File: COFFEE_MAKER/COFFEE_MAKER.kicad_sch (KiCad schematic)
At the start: 8 parts, among them U1 AZ1117IH-3.3TRG1, U2 AZ1117IH-5TRG1

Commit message: updated schematics
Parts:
- added C10, C9: C, symbol Device:C
- added C13, C14: C_Polarized_US, symbol Device:C_Polarized_US
- added C16: 100nF, symbol Device:C
- added C17: 10uF, symbol Device:C
- added C18, C20, C21: .1uF, symbol Device:C
- added C19: 1uF, symbol Device:C
- added D1: LED, symbol Device:LED
- added D7, D8: 1N4148, Diode_THT:D_DO-35_SOD27_P7.62mm_Horizontal, symbol Diode:1N4148
- added DS1: HY1602E, Display:HY1602E, symbol Display_Character:HY1602E
- added FB1, FB2: FerriteBead_Small, symbol Device:FerriteBead_Small
- added J2: Conn_01x06, symbol Connector_Generic:Conn_01x06
- added J3, J6: Conn_01x02_Pin, Connector_PinHeader_2.54mm:PinHeader_1x02_P2.54mm_Vertical, symbol Connector:Conn_01x02_Pin
- added J4: Screw_Terminal_01x02, symbol Connector:Screw_Terminal_01x02
- added J5: USB_C_Receptacle_USB2.0, symbol Connector:USB_C_Receptacle_USB2.0
- added J7: Conn_01x04, symbol Connector_Generic:Conn_01x04
- added JP1: A0, symbol Jumper:SolderJumper_2_Open
- added JP2: A1, symbol Jumper:SolderJumper_2_Open
- added JP3: A2, symbol Jumper:SolderJumper_2_Open
- added JP4: Jumper_2_Open, symbol Jumper:Jumper_2_Open
- added Q1: BC850, Package_TO_SOT_SMD:SOT-23, symbol Transistor_BJT:BC850
- added R10: 10k, symbol Device:R
- added R11, R12, R13, R14, R3, R4, R5, R6, R7: R, symbol Device:R
- added R8, R9: 5.1 k, symbol Device:R
- added RV1: potentiometer, Potentiometer_SMD:Potentiometer_ACP_CA9-VSMD_Vertical_Hole, symbol Device:R_Potentiometer_Trim
- added SW5: Reset, symbol Switch:SW_Omron_B3FS
- added SW6: Boot, symbol Switch:SW_Omron_B3FS
- added U4: PCF8574, symbol Interface_Expansion:PCF8574
- added U5: MAX31855KASA, Package_SO:SOIC-8_3.9x4.9mm_P1.27mm, symbol Sensor_Temperature:MAX31855KASA
- added U6: L78L33_SOT89, Package_TO_SOT_SMD:SOT-89-3, symbol Regulator_Linear:L78L33_SOT89
- added U7: LD1117S33TR_SOT223, Package_TO_SOT_SMD:SOT-223-3_TabPin2, symbol Regulator_Linear:LD1117S33TR_SOT223
- added U8: ESP32-S2-SOLO, PCM_Espressif:ESP32-S2-SOLO, symbol esp32:ESP32-S2-SOLO
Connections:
- net +3.3V: now also C17.1, C19.2, C20.2, R10.1, U7.2 (VO), U8.2 (3V3)
- net +5V: now also C10.1, C16.1, DS1.4 (VDD), J2.6 (Pin_6), J5.A4 (VBUS), J5.A9 (VBUS), J5.B4 (VBUS), J5.B9 (VBUS), J7.2 (Pin_2), JP4.2 (B), R11.1, R12.1, R13.2, R14.1, R5.1, R6.1, R7.1, RV1.1, U4.16 (VDD), U6.3 (IN), U7.3 (VI)
- net GND: now also C10.2, C13.2, C14.2, C16.2, C17.2, C18.1, C19.1, C20.1, C21.2, D1.1 (K), DS1.3 (VSS), J2.4 (Pin_4), J3.1 (Pin_1), J5.A1 (GND), J5.A12 (GND), J5.B1 (GND), J5.B12 (GND), J5.S1 (SHIELD), J6.1 (Pin_1), J7.1 (Pin_1), JP1.1 (A), JP2.1 (A), JP3.1 (A), Q1.2 (E), R8.2, R9.1, RV1.3, SW5.1, SW6.2, U4.8 (VSS), U5.1 (GND), U6.2 (GND), U7.1 (GND), U8.1 (GND), U8.40 (GND), U8.41 (GND)
- new net: J5.A5 (CC1), R8.1
- new net: J7.3 (Pin_3), R11.2, U4.14 (SCL)
- new net: DS1.5 (Vo), RV1.2
- new net: JP1.2 (B), R5.2, U4.1 (A0)
- new net: FB1.1, J4.1 (Pin_1)
- new net: FB2.2, J4.2 (Pin_2)
- new net: DS1.14 (DB5), U4.10 (P5)
- new net: DS1.15 (DB6), U4.11 (P6)
- new net: DS1.16 (DB7), U4.12 (P7)
- new net: J7.4 (Pin_4), R12.2, U4.15 (SDA)
- new net: JP2.2 (B), R6.2, U4.2 (A1)
- new net: JP3.2 (B), R7.2, U4.3 (A2)
- new net: DS1.6 (RS), U4.4 (P0)
- new net: DS1.7 (R/~{W}), U4.5 (P1)
- new net: DS1.8 (E), U4.6 (P2)
- new net: Q1.1 (B), R14.2, U4.7 (P3)
- new net: DS1.13 (DB4), U4.9 (P4)
- new net: DS1.2 (LEDA), JP4.1 (A)
- new net: J5.B5 (CC2), R9.2
- new net: C9.1, FB2.1, U5.3 (T+)
- new net: C9.2, FB1.2, U5.2 (T-)
- new net: D7.2 (A), R4.2, U5.5 (SCK)
- new net: D8.2 (A), R3.1, U5.6 (~{CS})
- new net: J2.2 (Pin_2), U5.7 (SO)
- new net: C21.1, SW6.1, U8.27 (GPIO0)
- new net: C18.2, R10.2, SW5.2, U8.3 (EN)
- new net: DS1.1 (LEDK), Q1.3 (C)
- new net: D7.1 (K), J2.1 (Pin_1)
- new net: D8.1 (K), J2.3 (Pin_3)
- new net: D1.2 (A), R13.1
- new net +3V3: C13.1, C14.1, J2.5 (Pin_5), R3.2, R4.1, U5.4 (V_CC), U6.1 (OUT)
- new net D+: J5.A6 (D+), J5.B6 (D+)
- new net D-: J5.A7 (D-), J5.B7 (D-)
- no-connect marks 6 -> 4
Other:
- removed sheet ESP32-S3-WROOM-1-Breakout
- added sheet Untitled Sheet (untitled.kicad_sch)
- note added: "3.3V Supply"
- note added: "ESP32S2"
- note added: "Fan"
- note added: "Heating Coil"
- note added: "LCD I2C"
- note added: "USB_Connector"
- note added: "thermocouple module"
- note removed: "Voltage Regulators Overcurrent/ Overvoltage Protection"

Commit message: schematics update
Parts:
- removed J7: Conn_01x04, symbol Connector_Generic:Conn_01x04
- added J1: Conn_01x04, symbol Connector_Generic:Conn_01x04
- U1, U2: footprint AZ1117IH-3:SOT223_AZ1117I_6P5X3P5_DIO -> AZ1117IH-3.3TRG1:SOT230P700X185-4N; Purchase-URL https://www.snapeda.com/api/url_track_click_mouser/?unipart_id=490259&manufacturer=Diodes Inc.&part_name=AZ1117IH-3.3TRG1&search_term=az1117ih-3.3trg1 -> https://www.snapeda.com/api/url_track_click_mouser/?unipart_id=490259&manufacturer=Diodes Inc.&part_name=AZ1117IH-3.3TRG1&search_term=None
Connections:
- net +5V is gone; now on net +3V3: C10.1, C16.1, C4.2, DS1.4 (VDD), F2.2, J2.6 (Pin_6), J5.A4 (VBUS), J5.A9 (VBUS), J5.B4 (VBUS), J5.B9 (VBUS), JP4.2 (B), R11.1, R12.1, R13.2, R14.1, R5.1, R6.1, R7.1, RV1.1, U4.16 (VDD), U6.3 (IN), U7.3 (VI)
- net GND is gone; now on net +3V3: C1.1, C10.2, C13.2, C14.2, C16.2, C17.2, C18.1, C19.1, C2.1, C20.1, C21.2, C3.1, C4.1, D1.1 (K), DS1.3 (VSS), J2.4 (Pin_4), J3.1 (Pin_1), J5.A1 (GND), J5.A12 (GND), J5.B1 (GND), J5.B12 (GND), J5.S1 (SHIELD), J6.1 (Pin_1), JP1.1 (A), JP2.1 (A), JP3.1 (A), Q1.2 (E), R8.2, R9.1, RV1.3, SW5.1, SW6.2, U1.1 (GND), U2.1 (GND), U4.8 (VSS), U5.1 (GND), U6.2 (GND), U7.1 (GND), U8.1 (GND), U8.40 (GND), U8.41 (GND)
- net +3V3: now also R11.2, R12.2, U4.14 (SCL), U4.15 (SDA), U8.12 (GPIO8/TOUCH8/ADC1_CH7), U8.17 (GPIO9/TOUCH9/ADC1_CH8/FSPIHD), J1.1 (Pin_1), J1.2 (Pin_2), J1.3 (Pin_3), J1.4 (Pin_4)
- net V_ALL+: now also J3.2 (Pin_2), J6.2 (Pin_2)
- net TC_so: now reaches J2.2 (Pin_2), U5.7 (SO)
- net TC_so: now also U8.21 (GPIO13/TOUCH13/ADC2_CH2/FSPIQ/FSPIIO7)
- net TC_cs: now reaches U8.10 (GPIO17/U1TXD/ADC2_CH6/DAC_1)
- net TC_cs: now also D8.1 (K), J2.3 (Pin_3)
- net TC_sck: now reaches U8.20 (GPIO12/TOUCH12/ADC2_CH1/FSPICLK/FSPIIO6)
- net TC_sck: now also D7.1 (K), J2.1 (Pin_1)
- no-connect marks 4 -> 39

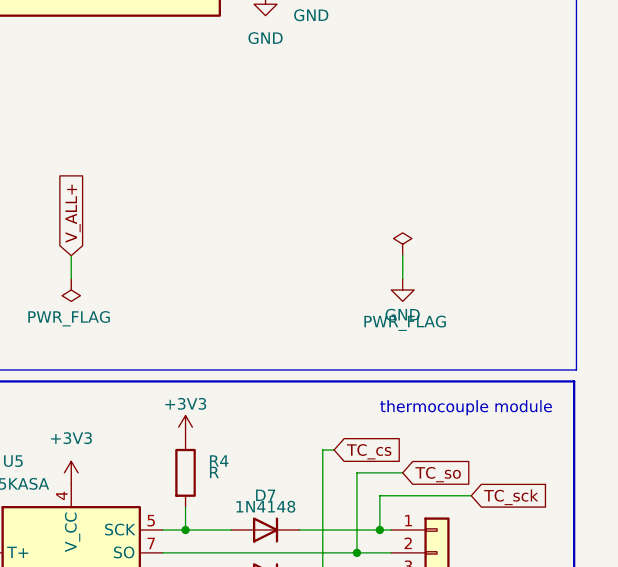
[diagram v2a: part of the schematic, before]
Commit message: schematics update
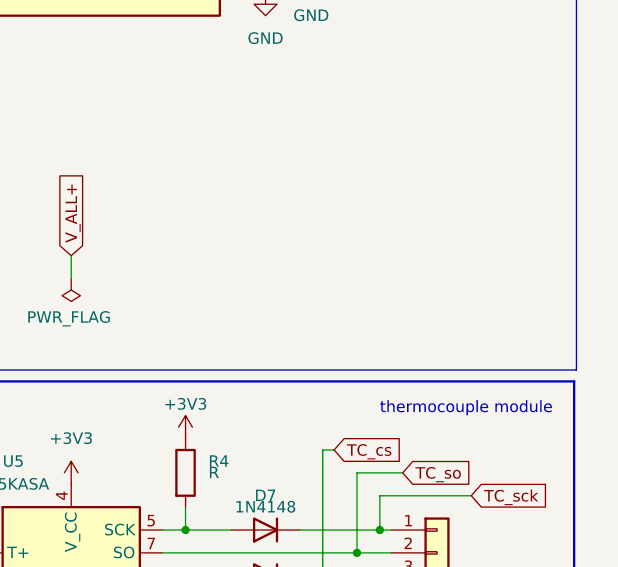
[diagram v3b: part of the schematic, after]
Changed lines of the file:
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@@
-    (stroke (width 0) (type default))
-  )
-  (wire (pts (xy 264.16 95.25) (xy 264.16 97.79))
     (stroke (width 0) (type default))
   )
@@
     )
   )
-  (symbol (lib_id "power:PWR_FLAG") (at 264.16 95.25 0) (unit 1)
-    (in_bom yes) (on_board yes) (dnp no)
-    (property "Reference" "#FLG04" (at 264.16 93.345 0)
-      (effects (font (size 1.27 1.27)) hide)
-    )
-    (property "Value" "PWR_FLAG" (at 264.414 102.616 0)
-      (effects (font (size 1.27 1.27)))
-    )
-    (property "Footprint" "" (at 264.16 95.25 0)
-      (effects (font (size 1.27 1.27)) hide)
-    )
-    (property "Datasheet" "~" (at 264.16 95.25 0)
-      (effects (font (size 1.27 1.27)) hide)
-    )
-    (pin "1")
-    (instances
-      (project "COFFEE_MAKER"
-        (path "/d1855ae5-bac9-4f6d-b11e-fad99d05f143"
-          (reference "#FLG04") (unit 1)
-        )
-      )
-    )
-  )
   (symbol (lib_id "power:GND") (at 227.33 140.97 0) (unit 1)
     (in_bom yes) (on_board yes) (dnp no) (fields_autoplaced)
@@
         )
       )
-    )
-  )
-  (symbol (lib_id "power:GND") (at 264.16 97.79 0) (unit 1)
-    (in_bom yes) (on_board yes) (dnp no)
-    (property "Reference" "#PWR012" (at 264.16 104.14 0)
-      (effects (font (size 1.27 1.27)) hide)
-    )
-    (property "Value" "GND" (at 264.16 101.854 0)
-      (effects (font (size 1.27 1.27)))
-    )
-    (property "Footprint" "" (at 264.16 97.79 0)
-      (effects (font (size 1.27 1.27)) hide)
-    )
-    (property "Datasheet" "" (at 264.16 97.79 0)
-      (effects (font (size 1.27 1.27)) hide)
-    )
-    (pin "1")
-    (instances
-      (project "COFFEE_MAKER"
-        (path "/d1855ae5-bac9-4f6d-b11e-fad99d05f143"
-          (reference "#PWR012") (unit 1)
-        )
-      )

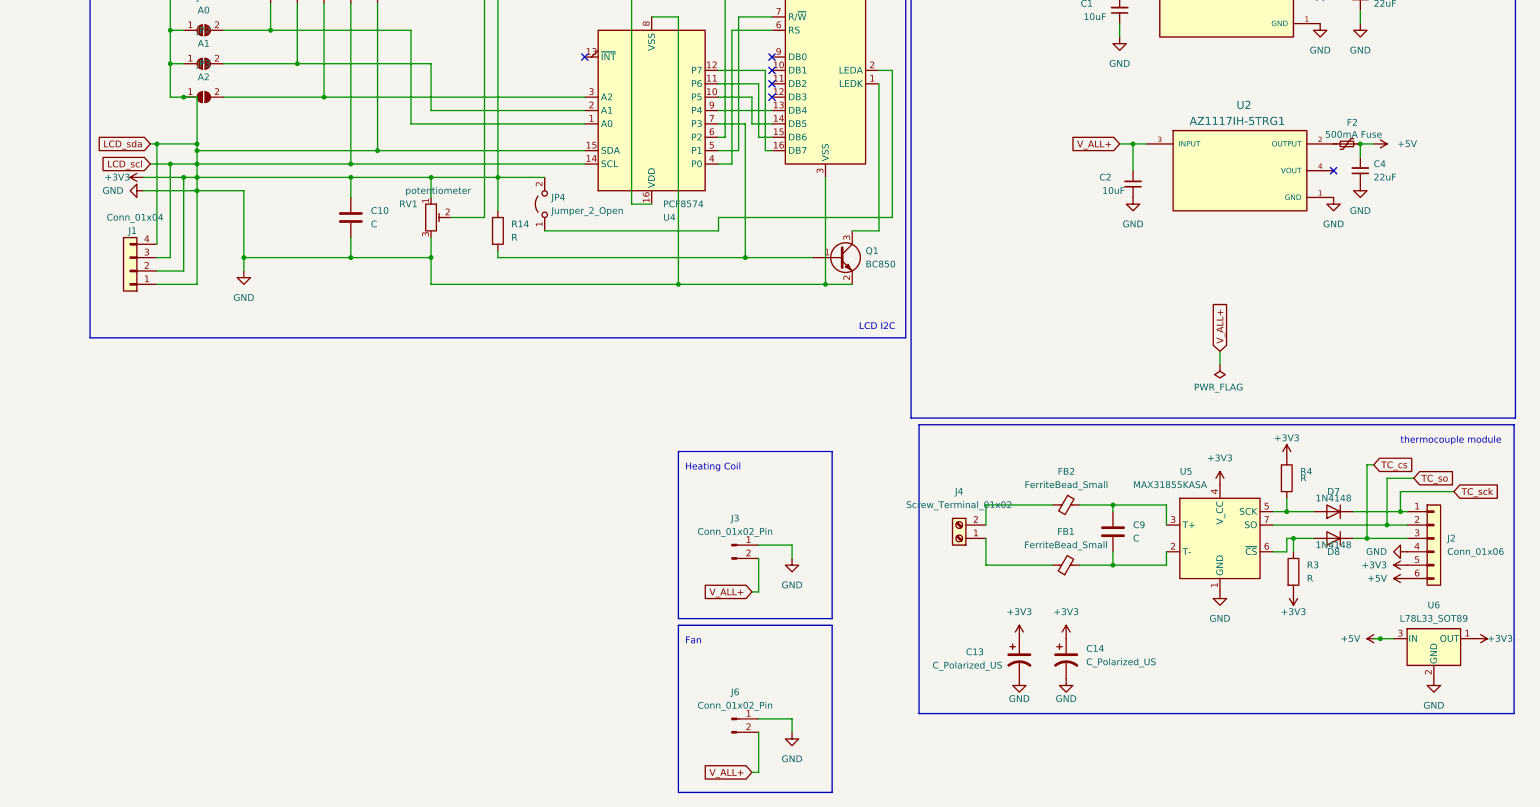
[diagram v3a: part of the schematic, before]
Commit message: schematic update
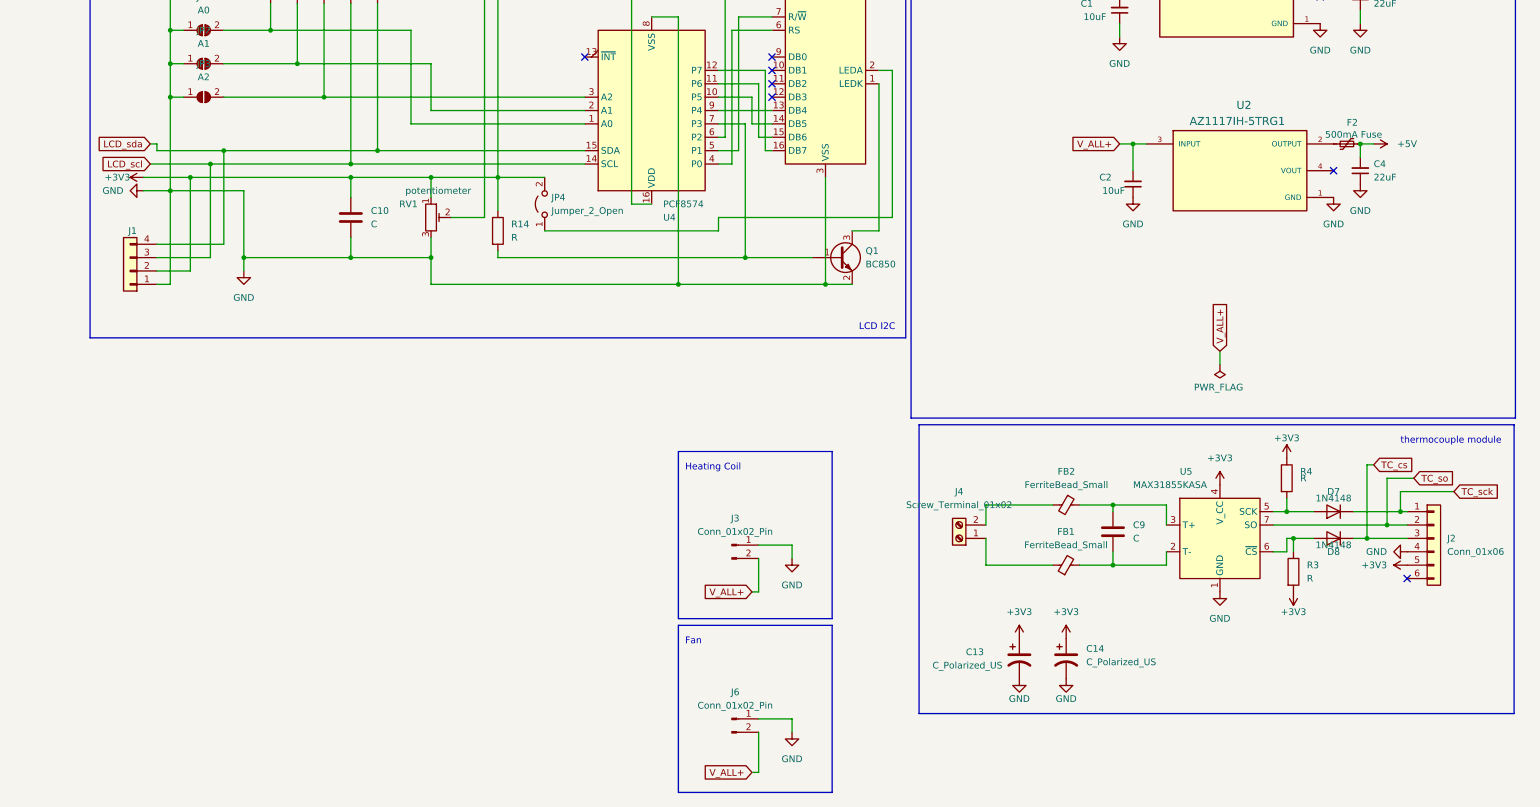
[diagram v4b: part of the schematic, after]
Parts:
- removed U6: L78L33_SOT89, Package_TO_SOT_SMD:SOT-89-3, symbol Regulator_Linear:L78L33_SOT89
- J5: footprint (none) -> Connector_USB:USB_C_Receptacle_GCT_USB4125-xx-x_6P_TopMnt_Horizontal
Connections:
- net +3V3: no longer C1.1, C10.2, C13.2, C14.2, C16.2, C17.2, C18.1, C19.1, C2.1, C20.1, C21.2, C3.1, C4.1, D1.1 (K), DS1.3 (VSS), J1.1 (Pin_1), J1.3 (Pin_3), J1.4 (Pin_4), J2.4 (Pin_4), J2.6 (Pin_6), J3.1 (Pin_1), J5.A1 (GND), J5.A12 (GND), J5.B1 (GND), J5.B12 (GND), J5.S1 (SHIELD), J6.1 (Pin_1), JP1.1 (A), JP2.1 (A), JP3.1 (A), Q1.2 (E), R11.2, R12.2, R8.2, R9.1, RV1.3, SW5.1, SW6.2, U1.1 (GND), U2.1 (GND), U4.14 (SCL), U4.15 (SDA), U4.8 (VSS), U5.1 (GND), U7.1 (GND), U8.1 (GND), U8.12 (GPIO8/TOUCH8/ADC1_CH7), U8.17 (GPIO9/TOUCH9/ADC1_CH8/FSPIHD), U8.40 (GND), U8.41 (GND)
- new net GND: C1.1, C10.2, C13.2, C14.2, C16.2, C17.2, C18.1, C19.1, C2.1, C20.1, C21.2, C3.1, C4.1, D1.1 (K), DS1.3 (VSS), J1.1 (Pin_1), J2.4 (Pin_4), J3.1 (Pin_1), J5.A1 (GND), J5.A12 (GND), J5.B1 (GND), J5.B12 (GND), J5.S1 (SHIELD), J6.1 (Pin_1), JP1.1 (A), JP2.1 (A), JP3.1 (A), Q1.2 (E), R8.2, R9.1, RV1.3, SW5.1, SW6.2, U1.1 (GND), U2.1 (GND), U4.8 (VSS), U5.1 (GND), U7.1 (GND), U8.1 (GND), U8.40 (GND), U8.41 (GND)
- new net LCD_scl: J1.3 (Pin_3), R11.2, U4.14 (SCL), U8.17 (GPIO9/TOUCH9/ADC1_CH8/FSPIHD)
- new net LCD_sda: J1.4 (Pin_4), R12.2, U4.15 (SDA), U8.12 (GPIO8/TOUCH8/ADC1_CH7)
- no-connect marks 39 -> 40

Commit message: schematic update
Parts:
- removed J5: USB_C_Receptacle_USB2.0, Connector_USB:USB_C_Receptacle_GCT_USB4125-xx-x_6P_TopMnt_Horizontal, symbol Connector:USB_C_Receptacle_USB2.0
- removed U1: AZ1117IH-3.3TRG1, AZ1117IH-3.3TRG1:SOT230P700X185-4N, symbol AZ1117IH-3.3TRG1:AZ1117IH-3.3TRG1
- removed U2: AZ1117IH-5TRG1, AZ1117IH-3.3TRG1:SOT230P700X185-4N, symbol AZ1117IH-3.3TRG1:AZ1117IH-3.3TRG1
- added J5: USB_C_Receptacle_USB2.0_16P, symbol Connector:USB_C_Receptacle_USB2.0_16P
- added U3: AMS1117-3.3, Package_TO_SOT_SMD:SOT-223-3_TabPin2, symbol Regulator_Linear:AMS1117-3.3
- added U6: AMS1117-5.0, Package_TO_SOT_SMD:SOT-223-3_TabPin2, symbol Regulator_Linear:AMS1117-5.0
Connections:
- net +3V3: now also U4.8 (VSS), J5.A4 (VBUS), J5.A9 (VBUS), J5.B4 (VBUS), J5.B9 (VBUS); no longer U4.16 (VDD)
- net D+: now also U8.14 (GPIO20/U1CTS/ADC2_CH9/CLK_OUT1/USB_D+), J5.A6 (D+), J5.B6 (D+)
- net D-: now also U8.13 (GPIO19/U1RTS/ADC2_CH8/CLK_OUT2/USB_D-), J5.A7 (D-), J5.B7 (D-)
- net GND: now also J5.A1 (GND), J5.A12 (GND), J5.B1 (GND), J5.B12 (GND), J5.S1 (SHIELD), U3.1 (GND), U6.1 (GND); no longer U4.8 (VSS)
- net V_ALL+: now also U3.3 (VI), U6.3 (VI)
- net at R8.1: now also J5.A5 (CC1)
- net at F1.1: now also U3.2 (VO)
- net at F2.1: now also U6.2 (VO)
- net at Q1.1 (B), R14.2, U4.7 (P3): now also U4.16 (VDD)
- net at R9.2: now also J5.B5 (CC2)
- no-connect marks 40 -> 36
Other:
- moved on the sheet: C3, F1
